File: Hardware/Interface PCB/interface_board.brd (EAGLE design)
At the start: 160 x 100 mm, 13 parts

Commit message: Interface board
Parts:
- removed D1: PURPLE, SparkFun-LED:LED-1206
- removed PRGM: SWITCH-MOMENTARY-2SMD-REDUNDANT, SparkFun-Electromechanical:TACTILE-SWITCH-SMD
- added JP2, JP4: (no value), pinhead:1X03
- added JP3: (no value), pinhead:2X04
- added PWR: PURPLE, SparkFun-LED:LED-1206
- added R10, R11, R3, R4, R5, R6, R7, R8, R9: 10k, rcl:R1206
- added S1: PRGM, switch-dil:SD4-01
- added SJ1, SJ2, SJ3, SJ4: (no value), jumper:SJ
- added U1, U2, U3, U4: BSS138-7-F, bss138_sot_23:SOT95P240X110-3N
- C1: device rcl:153CLV-0605 -> rcl:E2-5
- C3: value 680-1000uF -> 680uF
- moved RESET 116.3 mm to (-6.35, 44.5)
- moved R2 115.3 mm to (-14.0, 38.1)
- moved C3 89.5 mm to (29.2, 43.2)
- moved C5 82.0 mm to (-6.35, 38.1)
- moved JP1 79.2 mm to (-1.27, 17.8), turned to 90 degrees
- moved C4 72.3 mm to (-6.35, 33.0)
- moved NCP1117-3.3V 65.9 mm to (16.5, 43.2)
- moved U$1 62.2 mm to (39.4, 14.0), turned to 270 degrees
- moved R1 55.5 mm to (-19.1, 8.89)
- moved C2 31.4 mm to (-6.35, 3.81)
- moved C1 24.5 mm to (5.08, 40.6), turned to 180 degrees
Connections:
- net N$1 renamed ADC
- net N$10 renamed GPIO15
- net N$12 renamed RESET
- net N$5 renamed GPIO4
- net N$8 renamed GPIO13
- removed net N$11: JP1.16, U$1.GPIO16
- removed net N$3: JP1.4, PRGM.1, PRGM.2, U$1.GPIO0
- removed net N$4: JP1.5, U$1.GPIO2
- removed net N$9: JP1.14, U$1.GPIO14
- new net CH_PD: JP3.6, U$1.CH_PD
- new net GPIO0: JP1.4, JP3.3, R3.1, S1.2, U$1.GPIO0
- new net GPIO12: JP1.11, U$1.GPIO12
- new net GPIO14: JP1.14, R9.1, U$1.GPIO14, U4.2
- new net GPIO16: JP1.16, JP3.4, U$1.GPIO16
- new net GPIO2: JP1.5, JP3.5, R8.1, U$1.GPIO2, U3.2
- new net GPIO5: JP1.8, U$1.GPIO5
- new net RX: JP3.1, R5.1, SJ3.1, U$1.RX, U2.2
- new net RX_EXT: R7.1, SJ4.1, U2.3
- new net SCL: R11.1, U4.3
- new net SDA: R10.1, U3.3
- new net TX: JP3.8, R4.1, SJ1.2, U$1.TX, U1.2
- new net TX_EXT: R6.1, SJ2.2, U1.3
- net +3V3: now also JP3.2, JP4.3, R3.2, R4.2, R5.2, R8.2, R9.2, U1.1, U2.1, U3.1, U4.1
- net +5V: now also JP4.2, R10.2, R11.2, R6.2, R7.2
- net GND: now also JP2.1, JP3.7, JP4.1, PWR.C; no longer D1.C, PRGM.3, PRGM.4
- net N$2: now also PWR.A; no longer D1.A
- net N$6: now also JP2.3, SJ1.1, SJ2.1; no longer JP1.11, U$1.GPIO5
- net N$7: now also JP2.2, SJ3.2, SJ4.2; no longer JP1.8, U$1.GPIO12
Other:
- board size 160 x 100 mm -> 49.5 x 49.5 mm

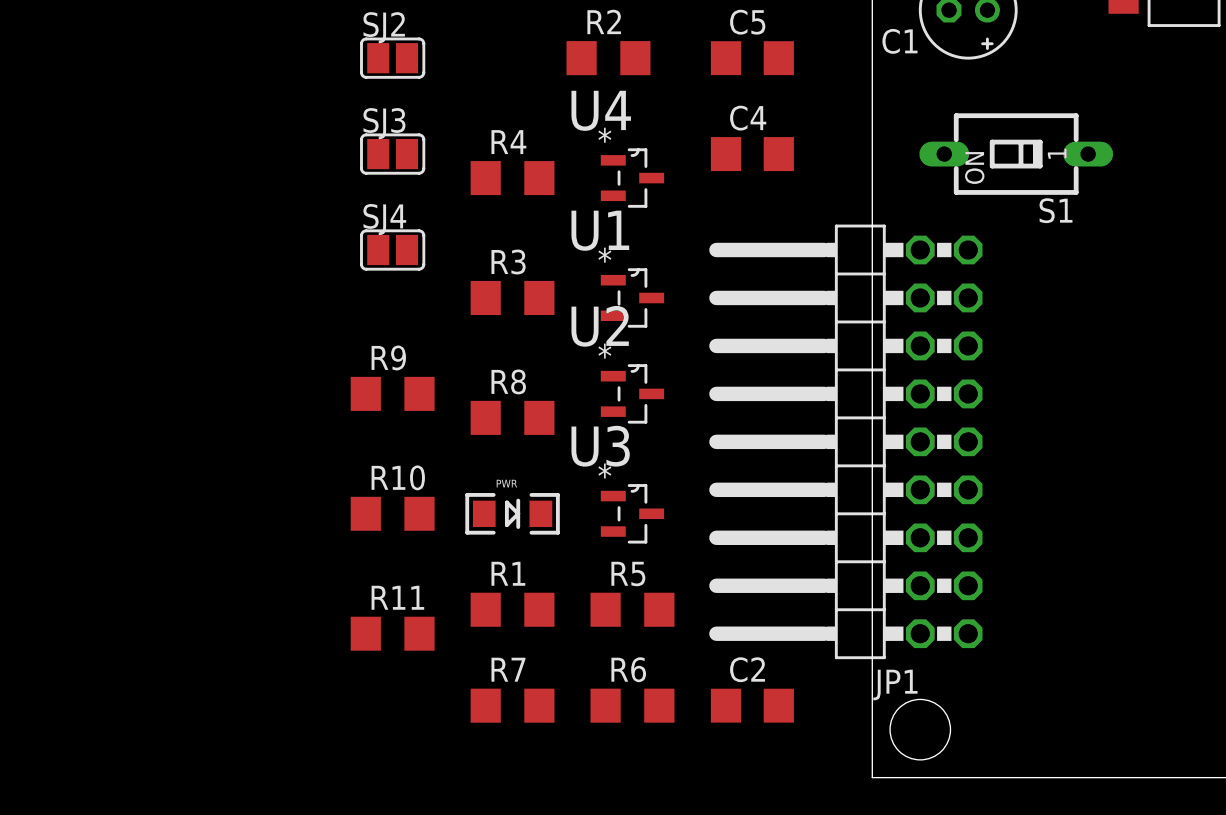
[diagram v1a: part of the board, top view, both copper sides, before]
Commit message: Main program
Added config file parser using ConfigParse, command-line parser using
argparse, logging, and signal handling. Finished UDP service discovery
process.
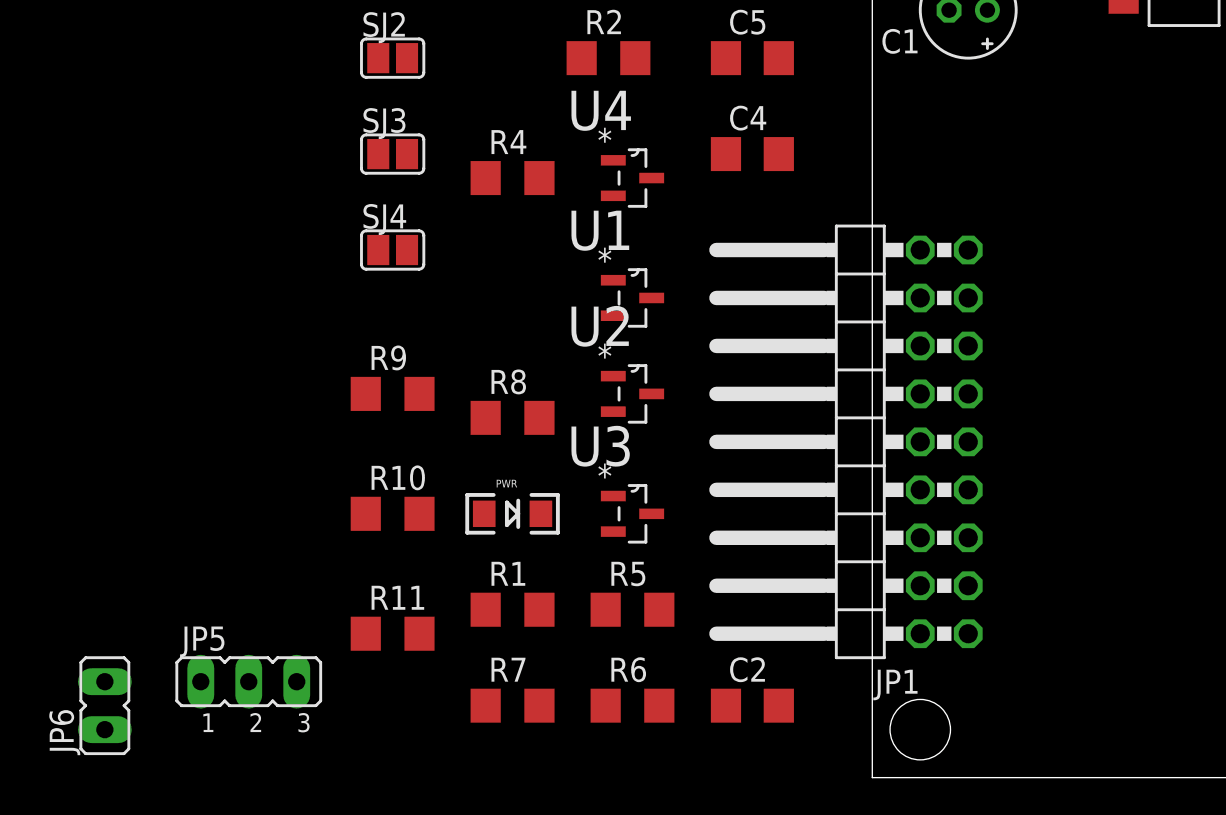
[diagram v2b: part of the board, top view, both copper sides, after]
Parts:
- removed R3: 10k, rcl:R1206
- removed S1: PRGM, switch-dil:SD4-01
- added JP5: (no value), jumper:JP2
- added JP6: (no value), jumper:JP1
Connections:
- new net GPIO0_EXT: JP1.4, JP5.1
- net +3V3: now also JP6.1; no longer R3.2
- net CH_PD: now also JP6.2
- net GND: now also JP5.3
- net GPIO0: now also JP5.2; no longer JP1.4, R3.1, S1.2
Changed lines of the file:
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@@
 <element name="R2" library="rcl" package="R1206" value="10k" x="-13.97" y="38.1"/>
 <element name="JP3" library="pinhead" package="2X04" value="" x="40.64" y="13.97"/>
-<element name="R3" library="rcl" package="R1206" value="10k" x="-19.05" y="25.4"/>
 <element name="U1" library="bss138_sot_23" package="SOT95P240X110-3N" value="BSS138-7-F" x="-12.7" y="25.4">
 <attribute name="PACKAGE" value="SOT-23-3" x="-12.7" y="25.4" size="1.778" layer="27" display="off"/>
@@
 <element name="R7" library="rcl" package="R1206" value="10k" x="-19.05" y="3.81"/>
 <element name="JP2" library="pinhead" package="1X03" value="" x="-16.51" y="43.18"/>
-<element name="S1" library="switch-dil" package="SD4-01" value="PRGM" x="7.62" y="33.02" rot="R90">
-<attribute name="OC_NEWARK" value="unknown" x="7.62" y="33.02" size="1.778" layer="27" rot="R90" display="off"/>
-<attribute name="MPN" value="" x="7.62" y="33.02" size="1.778" layer="27" rot="R90" display="off"/>
-<attribute name="MF" value="" x="7.62" y="33.02" size="1.778" layer="27" rot="R90" display="off"/>
-<attribute name="OC_FARNELL" value="unknown" x="7.62" y="33.02" size="1.778" layer="27" rot="R90" display="off"/>
-</element>
 <element name="SJ1" library="jumper" package="SJ" value="" x="-25.4" y="43.18"/>
 <element name="SJ2" library="jumper" package="SJ" value="" x="-25.4" y="38.1"/>
@@
 <element name="R10" library="rcl" package="R1206" value="10k" x="-25.4" y="13.97"/>
 <element name="R11" library="rcl" package="R1206" value="10k" x="-25.4" y="7.62"/>
+<element name="JP5" library="jumper" package="JP2" value="" x="-33.02" y="5.08"/>
+<element name="JP6" library="jumper" package="JP1" value="" x="-40.64" y="3.81"/>
 </elements>
 <signals>
@@
 <contactref element="JP2" pad="1"/>
 <contactref element="JP4" pad="1"/>
+<contactref element="JP5" pad="3"/>
 <wire x1="13.3096" y1="45.4914" x2="31.75" y2="43.18" width="0" layer="19" extent="1-1"/>
 <wire x1="4.064" y1="40.64" x2="13.3096" y2="45.4914" width="0" layer="19" extent="1-1"/>
 <wire x1="2.54" y1="46.99" x2="4.064" y2="40.64" width="0" layer="19" extent="1-1"/>
-<wire x1="5.08" y1="27.94" x2="4.064" y2="40.64" width="0" layer="19" extent="1-1"/>
+<wire x1="-3.556" y1="46.355" x2="2.54" y2="46.99" width="0" layer="19" extent="1-1"/>
+<wire x1="-9.144" y1="46.355" x2="-3.556" y2="46.355" width="0" layer="19" extent="1-1"/>
+<wire x1="-4.95" y1="38.1" x2="-3.556" y2="46.355" width="0" layer="19" extent="1-1"/>
+<wire x1="-4.95" y1="33.02" x2="-4.95" y2="38.1" width="0" layer="19" extent="1-1"/>
+<wire x1="-19.05" y1="43.18" x2="-9.144" y2="46.355" width="0" layer="19" extent="1-1"/>
+<wire x1="5.08" y1="27.94" x2="-4.95" y2="33.02" width="0" layer="19" extent="1-1"/>
 <wire x1="2.54" y1="20.32" x2="5.08" y2="27.94" width="0" layer="19" extent="1-1"/>
 <wire x1="2.54" y1="17.78" x2="2.54" y2="20.32" width="0" layer="19" extent="1-1"/>
@@
 <wire x1="5.08" y1="15.24" x2="5.08" y2="17.78" width="0" layer="19" extent="1-1"/>
 <wire x1="2.54" y1="7.62" x2="5.08" y2="15.24" width="0" layer="19" extent="1-1"/>
-<wire x1="-4.95" y1="38.1" x2="2.54" y2="7.62" width="0" layer="19" extent="1-1"/>
-<wire x1="-4.95" y1="33.02" x2="-4.95" y2="38.1" width="0" layer="19" extent="1-1"/>
-<wire x1="-17.55" y1="13.97" x2="2.54" y2="7.62" width="0" layer="19" extent="1-1"/>
-<wire x1="-3.556" y1="46.355" x2="-4.95" y2="33.02" width="0" layer="19" extent="1-1"/>
-<wire x1="-9.144" y1="46.355" x2="-3.556" y2="46.355" width="0" layer="19" extent="1-1"/>
-<wire x1="-19.05" y1="43.18" x2="-9.144" y2="46.355" width="0" layer="19" extent="1-1"/>
+<wire x1="-4.95" y1="3.81" x2="2.54" y2="7.62" width="0" layer="19" extent="1-1"/>
+<wire x1="-17.55" y1="13.97" x2="-4.95" y2="3.81" width="0" layer="19" extent="1-1"/>
+<wire x1="-30.48" y1="5.08" x2="-17.55" y2="13.97" width="0" layer="19" extent="1-1"/>
 <wire x1="31.265" y1="5.77" x2="5.08" y2="15.24" width="0" layer="19" extent="1-1"/>
 <wire x1="44.45" y1="12.7" x2="31.265" y2="5.77" width="0" layer="19" extent="1-1"/>
-<wire x1="-4.95" y1="3.81" x2="-4.95" y2="38.1" width="0" layer="19" extent="1-1"/>
 </signal>
 <signal name="+3V3">
@@
 <contactref element="R2" pad="2"/>
 <contactref element="JP3" pad="2"/>
-<contactref element="R3" pad="2"/>
 <contactref element="U1" pad="1"/>
 <contactref element="U2" pad="1"/>
@@
 <contactref element="R8" pad="2"/>
 <contactref element="R9" pad="2"/>
+<contactref element="JP6" pad="1"/>
 <wire x1="19.7104" y1="43.18" x2="26.67" y2="43.18" width="0" layer="19" extent="1-1"/>
 <wire x1="13.3096" y1="43.18" x2="19.7104" y2="43.18" width="0" layer="19" extent="1-1"/>
 <wire x1="7.62" y1="46.99" x2="13.3096" y2="43.18" width="0" layer="19" extent="1-1"/>
-<wire x1="2.54" y1="27.94" x2="13.3096" y2="43.18" width="0" layer="19" extent="1-1"/>
-<wire x1="5.08" y1="7.62" x2="2.54" y2="27.94" width="0" layer="19" extent="1-1"/>
-<wire x1="-17.628" y1="8.89" x2="5.08" y2="7.62" width="0" layer="19" extent="1-1"/>
-<wire x1="-11.278" y1="8.89" x2="-17.628" y2="8.89" width="0" layer="19" extent="1-1"/>
-<wire x1="-7.75" y1="38.1" x2="-11.278" y2="8.89" width="0" layer="19" extent="1-1"/>
+<wire x1="-7.75" y1="38.1" x2="7.62" y2="46.99" width="0" layer="19" extent="1-1"/>
+<wire x1="-12.548" y1="38.1" x2="-7.75" y2="38.1" width="0" layer="19" extent="1-1"/>
 <wire x1="-7.75" y1="33.02" x2="-7.75" y2="38.1" width="0" layer="19" extent="1-1"/>
-<wire x1="-17.628" y1="31.75" x2="-7.75" y2="38.1" width="0" layer="19" extent="1-1"/>
-<wire x1="-17.628" y1="25.4" x2="-17.628" y2="31.75" width="0" layer="19" extent="1-1"/>
-<wire x1="-13.716" y1="26.3398" x2="-17.628" y2="25.4" width="0" layer="19" extent="1-1"/>
+<wire x1="-13.716" y1="32.6898" x2="-12.548" y2="38.1" width="0" layer="19" extent="1-1"/>
+<wire x1="-17.628" y1="31.75" x2="-13.716" y2="32.6898" width="0" layer="19" extent="1-1"/>
+<wire x1="-13.716" y1="26.3398" x2="-13.716" y2="32.6898" width="0" layer="19" extent="1-1"/>
 <wire x1="-13.716" y1="21.2598" x2="-13.716" y2="26.3398" width="0" layer="19" extent="1-1"/>
-<wire x1="-13.716" y1="14.9098" x2="-13.716" y2="21.2598" width="0" layer="19" extent="1-1"/>
-<wire x1="-12.548" y1="38.1" x2="-7.75" y2="33.02" width="0" layer="19" extent="1-1"/>
-<wire x1="-13.716" y1="32.6898" x2="-12.548" y2="38.1" width="0" layer="19" extent="1-1"/>
-<wire x1="-23.978" y1="20.32" x2="-13.716" y2="26.3398" width="0" layer="19" extent="1-1"/>
-<wire x1="-17.628" y1="19.05" x2="-23.978" y2="20.32" width="0" layer="19" extent="1-1"/>
+<wire x1="-17.628" y1="19.05" x2="-13.716" y2="21.2598" width="0" layer="19" extent="1-1"/>
+<wire x1="-13.716" y1="14.9098" x2="-17.628" y2="19.05" width="0" layer="19" extent="1-1"/>
+<wire x1="-23.978" y1="20.32" x2="-17.628" y2="19.05" width="0" layer="19" extent="1-1"/>
+<wire x1="-11.278" y1="8.89" x2="-13.716" y2="14.9098" width="0" layer="19" extent="1-1"/>
+<wire x1="-17.628" y1="8.89" x2="-11.278" y2="8.89" width="0" layer="19" extent="1-1"/>
+<wire x1="2.54" y1="27.94" x2="-7.75" y2="33.02" width="0" layer="19" extent="1-1"/>
+<wire x1="5.08" y1="7.62" x2="-11.278" y2="8.89" width="0" layer="19" extent="1-1"/>
 <wire x1="31.265" y1="22.17" x2="26.67" y2="43.18" width="0" layer="19" extent="1-1"/>
 <wire x1="36.83" y1="15.24" x2="31.265" y2="22.17" width="0" layer="19" extent="1-1"/>
+<wire x1="-40.64" y1="2.54" x2="-17.628" y2="8.89" width="0" layer="19" extent="1-1"/>
 </signal>
 <signal name="N$2">
@@
 <contactref element="U$1" pad="CH_PD"/>
 <contactref element="JP3" pad="6"/>
+<contactref element="JP6" pad="2"/>
 <wire x1="41.91" y1="15.24" x2="41.17" y2="22.17" width="0" layer="19" extent="1-1"/>
+<wire x1="-40.64" y1="5.08" x2="41.91" y2="15.24" width="0" layer="19" extent="1-1"/>
 </signal>
 <signal name="TX">
@@
 <signal name="GPIO0">
 <contactref element="JP3" pad="3"/>
-<contactref element="JP1" pad="4"/>
 <contactref element="U$1" pad="GPIO0"/>
-<contactref element="R3" pad="1"/>
-<contactref element="S1" pad="2"/>
+<contactref element="JP5" pad="2"/>
 <wire x1="37.17" y1="5.77" x2="39.37" y2="12.7" width="0" layer="19" extent="1-1"/>
-<wire x1="2.54" y1="10.16" x2="37.17" y2="5.77" width="0" layer="19" extent="1-1"/>
-<wire x1="3.81" y1="33.02" x2="2.54" y2="10.16" width="0" layer="19" extent="1-1"/>
-<wire x1="-20.472" y1="25.4" x2="2.54" y2="10.16" width="0" layer="19" extent="1-1"/>
+<wire x1="-33.02" y1="5.08" x2="37.17" y2="5.77" width="0" layer="19" extent="1-1"/>
 </signal>
 <signal name="GPIO2">
@@
 <wire x1="-26.822" y1="13.97" x2="-11.684" y2="13.97" width="0" layer="19" extent="1-1"/>
 </signal>
+<signal name="GPIO0_EXT">
+<contactref element="JP5" pad="1"/>
+<contactref element="JP1" pad="4"/>
+<wire x1="2.54" y1="10.16" x2="-35.56" y2="5.08" width="0" layer="19" extent="1-1"/>
+</signal>
 </signals>
